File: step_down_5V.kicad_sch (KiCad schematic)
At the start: 30 parts, among them U2 TPS54202DDC

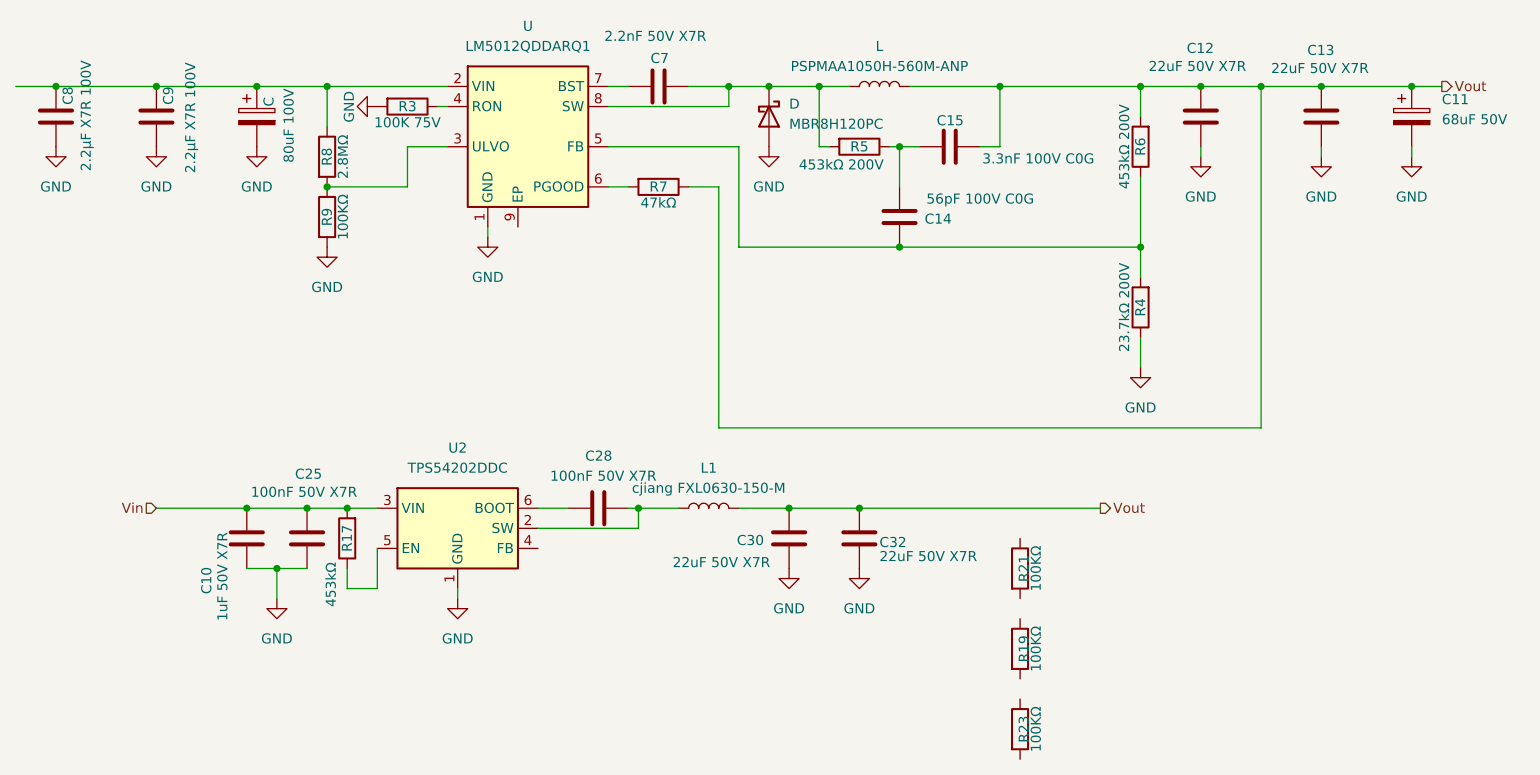
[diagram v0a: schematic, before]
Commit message: ADD: Terminado la fuente de 24V a 5V, terminado los pines del veronte y tambien el circuito de I2C
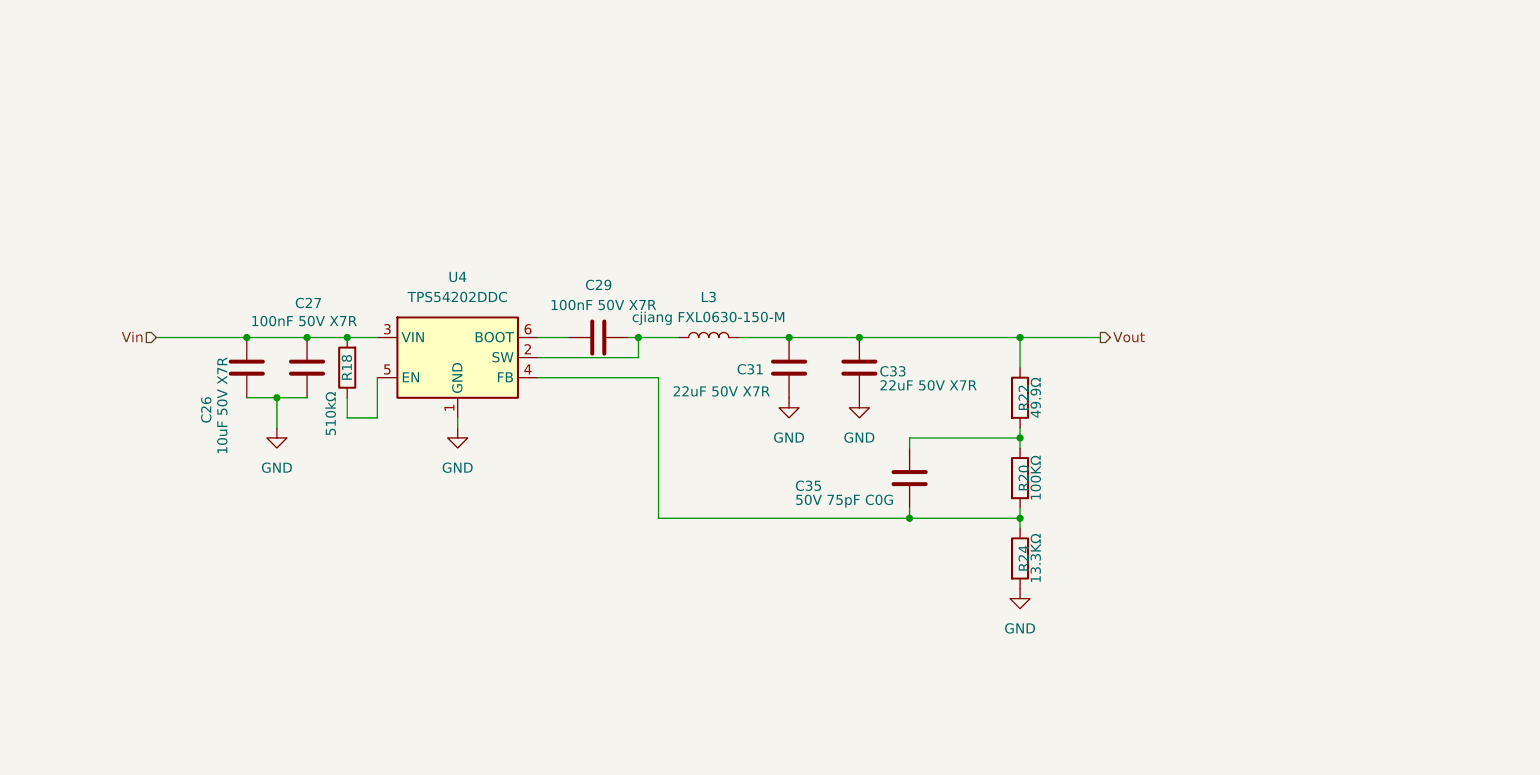
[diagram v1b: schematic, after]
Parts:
- removed C: 80uF 100V, Capacitor_SMD:CP_Elec_10x10.5, symbol Device:C_Polarized
- removed C11: 68uF 50V, Capacitor_SMD:CP_Elec_6.3x7.7, symbol Device:C_Polarized
- removed C12, C13: 22uF 50V X7R, Capacitor_SMD:C_1812_4532Metric, symbol Device:C
- removed C14: 56pF 100V C0G, Capacitor_SMD:C_0603_1608Metric, symbol Device:C
- removed C15: 3.3nF 100V C0G, Capacitor_SMD:C_1206_3216Metric, symbol Device:C
- removed C7: 2.2nF 50V X7R, Capacitor_SMD:C_0603_1608Metric, symbol Device:C
- removed C8, C9: 2.2µF X7R 100V, Capacitor_SMD:C_1206_3216Metric, symbol Device:C
- removed D: MBR8H120PC, Library:TO-277C, symbol Device:D_Schottky
- removed L: PSPMAA1050H-560M-ANP, Inductor_SMD:L_Sunlord_MWSA1005S, symbol Device:L
- removed R3: 100K 75V, Resistor_SMD:R_0603_1608Metric, symbol Device:R
- removed R4: 23.7kΩ 200V, Resistor_SMD:R_1206_3216Metric, symbol Device:R
- removed R5, R6: 453kΩ 200V, Resistor_SMD:R_1206_3216Metric, symbol Device:R
- removed R7: 47kΩ, Resistor_SMD:R_0805_2012Metric, symbol Device:R
- removed R8: 2.8MΩ, Resistor_SMD:R_1206_3216Metric, symbol Device:R
- removed R9: 100KΩ, Resistor_SMD:R_1206_3216Metric, symbol Device:R
- removed U: LM5012QDDARQ1, Package_SO:SOIC-8-1EP_3.9x4.9mm_P1.27mm_EP2.95x4.9mm_Mask2.71x3.4mm_ThermalVias, symbol 0_pdb_lib:LM5012QDDARQ1
- added C35: 50V 75pF C0G, Capacitor_SMD:C_0603_1608Metric, symbol Device:C
- C26: renamed from C10; value 1uF 50V X7R -> 10uF 50V X7R; footprint Capacitor_SMD:C_0603_1608Metric -> Capacitor_SMD:C_1206_3216Metric; LCSC Part # C5199872 -> C89632
- R18: renamed from R17; value 453kΩ -> 510kΩ; LCSC Part # C2085565 -> C17990
- R20: renamed from R19; LCSC Part # C17900 -> C728669
- R22: renamed from R21; value 100KΩ -> 49.9Ω; LCSC Part # C17900 -> C18018
- R24: renamed from R23; value 100KΩ -> 13.3KΩ; LCSC Part # C17900 -> C870412
- renumbered C25 to C27, C28 to C29, C30 to C31, C32 to C33, L1 to L3, U2 to U4
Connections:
- net GND: now also R24.2
- net Vout: now also R22.1
- net at R24.1: now also R20.2, U4.4 (FB), C35.1
- net at R20.1: now also R22.2, C35.2
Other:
- moved on the sheet: C26, C27, C29, C31, C33, L3, R18, R20, R22, R24, U4

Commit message: Primer sesion de ruteo
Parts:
- removed R18: 510kΩ, Resistor_SMD:R_1206_3216Metric, symbol Device:R
- renumbered C29 to C16, C26 to C17, C27 to C18, C31 to C19, C33 to C20, C35 to C21, L3 to L2, R22 to R13, R20 to R14, R24 to R15, U4 to U3
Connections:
- no-connect marks 0 -> 1
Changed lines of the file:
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@@
-	)
-	(junction
-		(at 104.14 50.8)
-		(diameter 0)
-		(color 0 0 0 0)
 	)
 	(junction
@@
 		(color 0 0 0 0)
 	)
+	(no_connect
+		(at 107.95 55.88)
+	)
 	(wire
 		(pts
@@
 	(wire
 		(pts
-			(xy 104.14 50.8) (xy 107.95 50.8)
+			(xy 99.06 50.8) (xy 107.95 50.8)
 		)
 		(stroke
@@
 	(wire
 		(pts
-			(xy 104.14 60.96) (xy 107.95 60.96)
-		)
-		(stroke
-			(width 0)
-			(type default)
-		)
-	)
-	(wire
-		(pts
 			(xy 95.25 62.23) (xy 95.25 58.42)
 		)
@@
 	(wire
 		(pts
-			(xy 99.06 50.8) (xy 104.14 50.8)
-		)
-		(stroke
-			(width 0)
-			(type default)
-		)
-	)
-	(wire
-		(pts
-			(xy 104.14 58.42) (xy 104.14 60.96)
-		)
-		(stroke
-			(width 0)
-			(type default)
-		)
-	)
-	(wire
-		(pts
 			(xy 118.11 62.23) (xy 118.11 60.96)
 		)
@@
 		(pts
 			(xy 128.27 50.8) (xy 132.08 50.8)
-		)
-		(stroke
-			(width 0)
-			(type default)
-		)
-	)
-	(wire
-		(pts
-			(xy 107.95 60.96) (xy 107.95 55.88)
 		)
 		(stroke
@@
 		(on_board yes)
 		(dnp no)
-		(property "Reference" "R24"
+		(property "Reference" "R15"
 			(at 189.738 78.74 90)
 			(effects
@@
 			(project "pdb"
 				(path "/402e9eb5-eedc-44fb-9e44-3f0a74044b6b/a179203d-47eb-4696-bef1-6d097b725168"
-					(reference "R24")
+					(reference "R15")
 					(unit 1)
 				)
@@
 		(dnp no)
 		(fields_autoplaced yes)
-		(property "Reference" "L3"
+		(property "Reference" "L2"
 			(at 149.86 45.72 90)
 			(effects
@@
 			(project "pdb"
 				(path "/402e9eb5-eedc-44fb-9e44-3f0a74044b6b/a179203d-47eb-4696-bef1-6d097b725168"
-					(reference "L3")
-					(unit 1)
-				)
-			)
-		)
-	)
-	(symbol
-		(lib_id "Device:R")
-		(at 104.14 54.61 180)
-		(unit 1)
-		(exclude_from_sim no)
-		(in_bom yes)
-		(on_board yes)
-		(dnp no)
-		(property "Reference" "R18"
-			(at 104.14 54.61 90)
-			(effects
-				(font
-					(size 1.27 1.27)
-				)
-			)
-		)
-		(property "Value" "510kΩ"
-			(at 102.108 60.452 90)
-			(effects
-				(font
-					(size 1.27 1.27)
-				)
-			)
-		)
-		(property "Footprint" "Resistor_SMD:R_1206_3216Metric"
-			(at 105.918 54.61 90)
-			(effects
-				(font
-					(size 1.27 1.27)
-				)
-				(hide yes)
-			)
-		)
-		(property "Datasheet" "~"
-			(at 104.14 54.61 0)
-			(effects
-				(font
-					(size 1.27 1.27)
-				)
-				(hide yes)
-			)
-		)
-		(property "Description" "Resistor"
-			(at 104.14 54.61 0)
-			(effects
-				(font
-					(size 1.27 1.27)
-				)
-				(hide yes)
-			)
-		)
-		(property "LCSC Part #" "C17990"
-			(at 104.14 54.61 90)
-			(effects
-				(font
-					(size 1.27 1.27)
-				)
-				(hide yes)
-			)
-		)
-		(pin "1"
-		)
-		(pin "2"
-		)
-		(instances
-			(project "pdb"
-				(path "/402e9eb5-eedc-44fb-9e44-3f0a74044b6b/a179203d-47eb-4696-bef1-6d097b725168"
-					(reference "R18")
+					(reference "L2")
 					(unit 1)
 				)
@@
 		(dnp no)
 		(fields_autoplaced yes)
-		(property "Reference" "#PWR071"
+		(property "Reference" "#PWR069"
 			(at 118.11 68.58 0)
 			(effects
@@
 			(project "pdb"
 				(path "/402e9eb5-eedc-44fb-9e44-3f0a74044b6b/a179203d-47eb-4696-bef1-6d097b725168"
-					(reference "#PWR071")
+					(reference "#PWR069")
 					(unit 1)
 				)
@@
 		(on_board yes)
 		(dnp no)
-		(property "Reference" "C29"
+		(property "Reference" "C16"
 			(at 137.668 44.196 90)
 			(effects
@@
 			(project "pdb"
 				(path "/402e9eb5-eedc-44fb-9e44-3f0a74044b6b/a179203d-47eb-4696-bef1-6d097b725168"
-					(reference "C29")
+					(reference "C16")
 					(unit 1)
 				)
@@
 		(dnp no)
 		(fields_autoplaced yes)
-		(property "Reference" "#PWR085"
+		(property "Reference" "#PWR070"
 			(at 189.23 88.9 0)
 			(effects
@@
 			(project "pdb"
 				(path "/402e9eb5-eedc-44fb-9e44-3f0a74044b6b/a179203d-47eb-4696-bef1-6d097b725168"
-					(reference "#PWR085")
+					(reference "#PWR070")
 					(unit 1)
 				)
@@
 		(on_board yes)
 		(dnp no)
-		(property "Reference" "C27"
+		(property "Reference" "C18"
 			(at 97.536 46.482 0)
 			(effects
@@
 			(project "pdb"
 				(path "/402e9eb5-eedc-44fb-9e44-3f0a74044b6b/a179203d-47eb-4696-bef1-6d097b725168"
-					(reference "C27")
+					(reference "C18")
 					(unit 1)
 				)
@@
 		(on_board yes)
 		(dnp no)
-		(property "Reference" "C35"
+		(property "Reference" "C21"
 			(at 160.782 69.596 0)
 			(effects
@@
 			(project "pdb"
 				(path "/402e9eb5-eedc-44fb-9e44-3f0a74044b6b/a179203d-47eb-4696-bef1-6d097b725168"
-					(reference "C35")
+					(reference "C21")
 					(unit 1)
 				)
@@
 		(dnp no)
 		(fields_autoplaced yes)
-		(property "Reference" "#PWR075"
+		(property "Reference" "#PWR067"
 			(at 168.91 64.77 0)
 			(effects
@@
 			(project "pdb"
 				(path "/402e9eb5-eedc-44fb-9e44-3f0a74044b6b/a179203d-47eb-4696-bef1-6d097b725168"
-					(reference "#PWR075")
+					(reference "#PWR067")
 					(unit 1)
 				)
@@
 		(on_board yes)
 		(dnp no)
-		(property "Reference" "R20"
+		(property "Reference" "R14"
 			(at 189.738 68.58 90)
 			(effects
@@
 			(project "pdb"
 				(path "/402e9eb5-eedc-44fb-9e44-3f0a74044b6b/a179203d-47eb-4696-bef1-6d097b725168"
-					(reference "R20")
+					(reference "R14")
 					(unit 1)
 				)
@@
 		(on_board yes)
 		(dnp no)
-		(property "Reference" "C31"
+		(property "Reference" "C19"
 			(at 153.416 54.864 0)
 			(effects
@@
 			(project "pdb"
 				(path "/402e9eb5-eedc-44fb-9e44-3f0a74044b6b/a179203d-47eb-4696-bef1-6d097b725168"
-					(reference "C31")
+					(reference "C19")
 					(unit 1)
 				)
@@
 		(on_board yes)
 		(dnp no)
-		(property "Reference" "C33"
+		(property "Reference" "C20"
 			(at 171.45 55.118 0)
 			(effects
@@
 			(project "pdb"
 				(path "/402e9eb5-eedc-44fb-9e44-3f0a74044b6b/a179203d-47eb-4696-bef1-6d097b725168"
-					(reference "C33")
+					(reference "C20")
 					(unit 1)
 				)
@@
 		(dnp no)
 		(fields_autoplaced yes)
-		(property "Reference" "U4"
+		(property "Reference" "U3"
 			(at 118.11 43.18 0)
 			(effects
@@
 				)
 				(path "/402e9eb5-eedc-44fb-9e44-3f0a74044b6b/a179203d-47eb-4696-bef1-6d097b725168"
-					(reference "U4")
+					(reference "U3")
 					(unit 1)
 				)
@@
 		(on_board yes)
 		(dnp no)
-		(property "Reference" "R22"
+		(property "Reference" "R13"
 			(at 189.738 58.42 90)
 			(effects
@@
 			(project "pdb"
 				(path "/402e9eb5-eedc-44fb-9e44-3f0a74044b6b/a179203d-47eb-4696-bef1-6d097b725168"
-					(reference "R22")
+					(reference "R13")
 					(unit 1)
 				)
@@
 		(dnp no)
 		(fields_autoplaced yes)
-		(property "Reference" "#PWR059"
+		(property "Reference" "#PWR068"
 			(at 95.25 68.58 0)
 			(effects
@@
 				)
 				(path "/402e9eb5-eedc-44fb-9e44-3f0a74044b6b/a179203d-47eb-4696-bef1-6d097b725168"
-					(reference "#PWR059")
+					(reference "#PWR068")
 					(unit 1)
 				)
@@
 		(on_board yes)
 		(dnp no)
-		(property "Reference" "C26"
+		(property "Reference" "C17"
 			(at 86.36 59.944 90)
 			(effects
@@
 			(project "pdb"
 				(path "/402e9eb5-eedc-44fb-9e44-3f0a74044b6b/a179203d-47eb-4696-bef1-6d097b725168"
-					(reference "C26")
+					(reference "C17")
 					(unit 1)
 				)
@@
 		(dnp no)
 		(fields_autoplaced yes)
-		(property "Reference" "#PWR073"
+		(property "Reference" "#PWR066"
 			(at 160.02 64.77 0)
 			(effects
@@
 			(project "pdb"
 				(path "/402e9eb5-eedc-44fb-9e44-3f0a74044b6b/a179203d-47eb-4696-bef1-6d097b725168"
-					(reference "#PWR073")
+					(reference "#PWR066")
 					(unit 1)
 				)

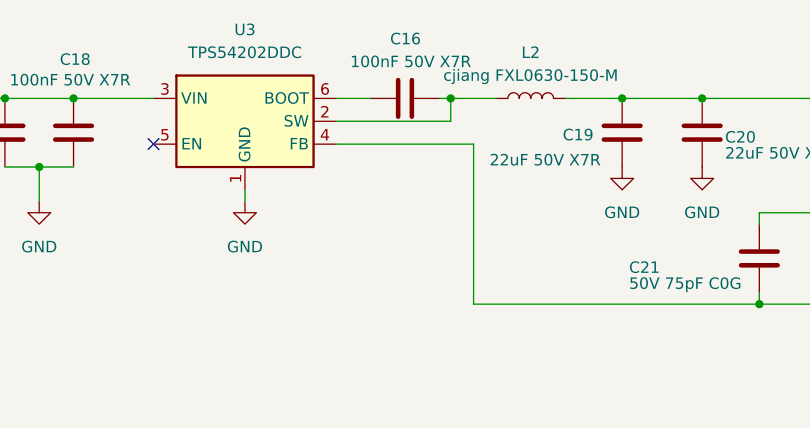
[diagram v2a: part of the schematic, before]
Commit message: Agregado los testpoint, falta leds indicadores y serigrafia y cerramos
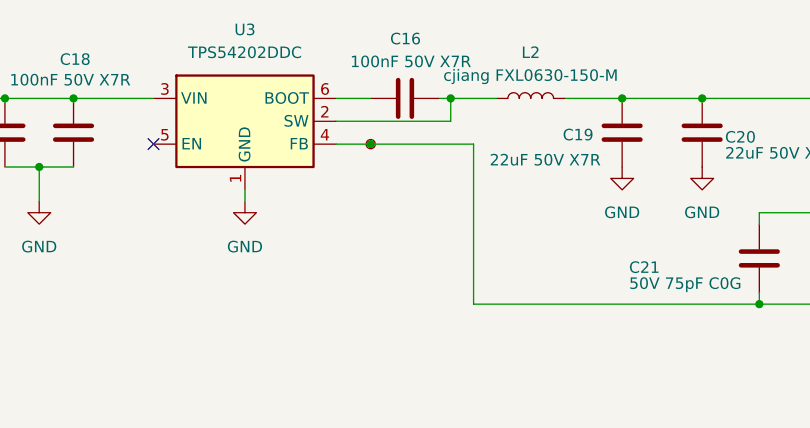
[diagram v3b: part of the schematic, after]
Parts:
- added TP26: FB_5V, 0_ZA_Lib:TestPoint_Pad_D2.0mm_silk_value, symbol Connector:TestPoint_Small
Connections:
- net at C21.1, R14.2, R15.1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: now also TP26.1
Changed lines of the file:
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@@
+	)
+	(junction
+		(at 132.08 55.88)
+		(diameter 0)
+		(color 0 0 0 0)
 	)
 	(junction
@@
 	(wire
 		(pts
-			(xy 128.27 55.88) (xy 143.51 55.88)
+			(xy 128.27 55.88) (xy 132.08 55.88)
 		)
 		(stroke
@@
 		(pts
 			(xy 175.26 73.66) (xy 189.23 73.66)
+		)
+		(stroke
+			(width 0)
+			(type default)
+		)
+	)
+	(wire
+		(pts
+			(xy 132.08 55.88) (xy 143.51 55.88)
 		)
 		(stroke
@@
 					(unit 1)
 				)
+			)
+		)
+	)
+	(symbol
+		(lib_id "Connector:TestPoint_Small")
+		(at 132.08 55.88 0)
+		(unit 1)
+		(exclude_from_sim no)
+		(in_bom yes)
+		(on_board yes)
+		(dnp no)
+		(property "Reference" "TP26"
+			(at 133.35 54.6099 0)
+			(effects
+				(font
+					(size 1.27 1.27)
+				)
+				(justify left)
+				(hide yes)
+			)
+		)
+		(property "Value" "FB_5V"
+			(at 145.542 54.864 0)
+			(effects
+				(font
+					(size 1.27 1.27)
+				)
+				(justify left)
+				(hide yes)
+			)
+		)
+		(property "Footprint" "0_ZA_Lib:TestPoint_Pad_D2.0mm_silk_value"
+			(at 137.16 55.88 0)
+			(effects
+				(font
+					(size 1.27 1.27)
+				)
+				(hide yes)
+			)
+		)
+		(property "Datasheet" "~"
+			(at 137.16 55.88 0)
+			(effects
+				(font
+					(size 1.27 1.27)
+				)
+				(hide yes)
+			)
+		)
+		(property "Description" "test point"
+			(at 132.08 55.88 0)
+			(effects
+				(font
+					(size 1.27 1.27)
+				)
+				(hide yes)
+			)
+		)
+		(pin "1"
+		)
+		(instances
+			(project "pdb"
+				(path "/402e9eb5-eedc-44fb-9e44-3f0a74044b6b/a179203d-47eb-4696-bef1-6d097b725168"
+					(reference "TP26")
+					(unit 1)
+				)
